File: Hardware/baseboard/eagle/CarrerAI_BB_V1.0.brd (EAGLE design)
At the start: 59 x 52 mm, 190 parts, among them J1 MICROUSB-FEM, X1 JST-4POS-2X4POS, X1.2 TACH/LAP, X2.2 VRAILS+, X2.3 5V+SoC

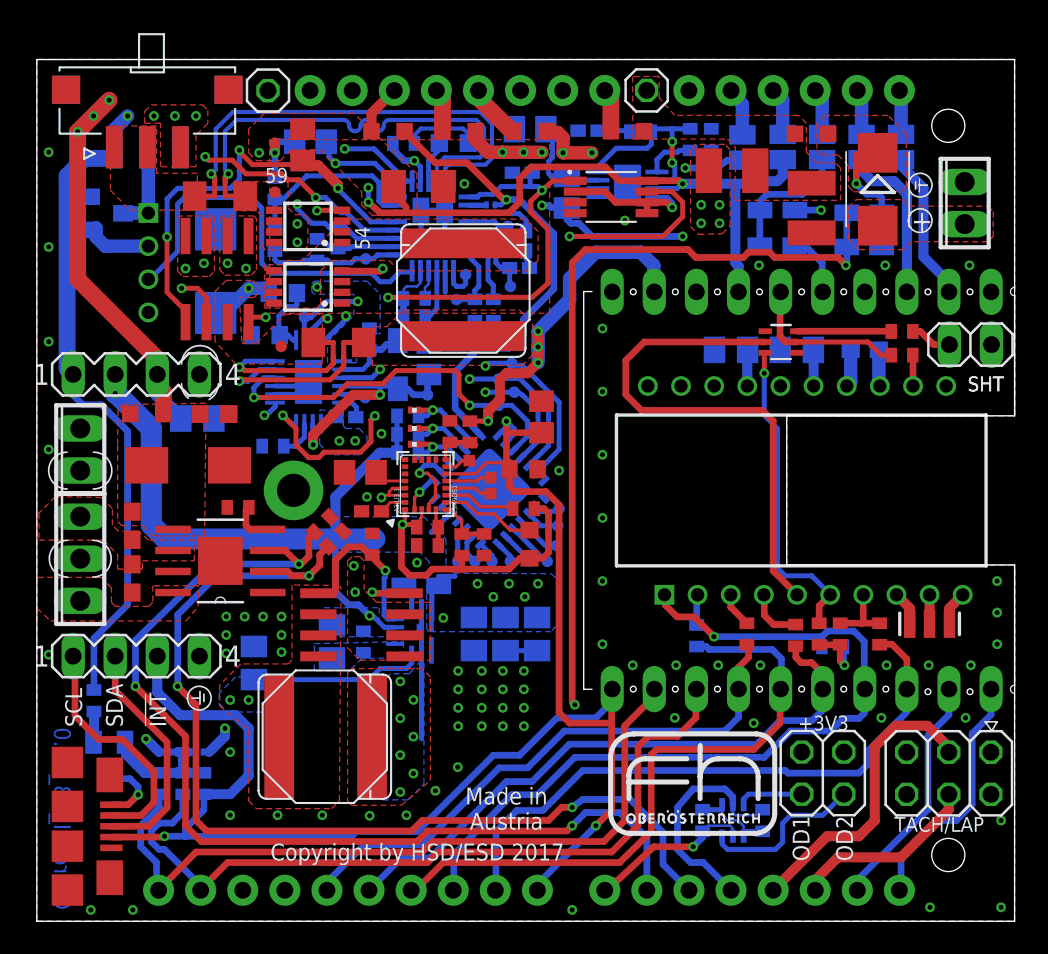
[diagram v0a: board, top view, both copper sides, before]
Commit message: CarrerAI_BB_V1.0: now diverging from original design  -> will drop the management IC in favor of 100mil pitch vias     as it will result in a better and more flexible design     (can be patched against SoC side I/O, or topped with IC)  -> I2C GPIO can be attached via a mezzaine board     (there's enough space)  -> will repurpose some vias as pins in this area,     which was the intention from the start actually thinking of it
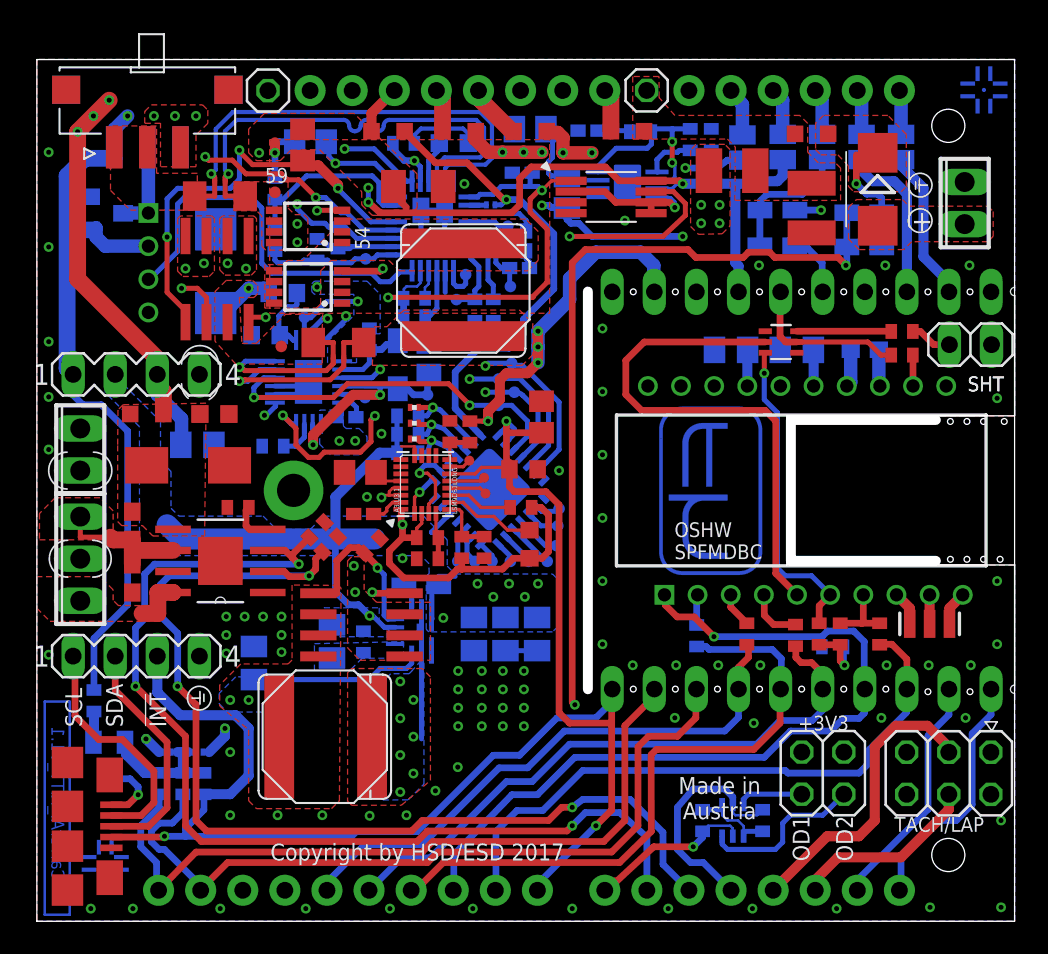
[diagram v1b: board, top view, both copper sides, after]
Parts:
- added U$1, U$2: (no value), marks:PASSER-CIRCLE
- A10:REF2: value REF.LOGO.UASUA -> REF.LOGO.UASUAS-GRADE; device kitt.refs:REF_LOGO_UASUA -> kitt.refs:DCL.LOGO.FHOOE-6MM-S
- A3:U3.1: value LSM9DS1 -> LSM9DS1LONG; device kitt.ic:LGA-24 -> kitt.ic:KITT.IC_LGA-24
- A3:☇1, A3:☇2, A3:☇3: value PTR1TP07SQ -> PTR1TP06R; device testpad:TP07SQ -> testpad:TP06R
- moved A10:REF2 22.5 mm to (40.6, 26.0), flipped to the bottom, turned to 270 degrees
- moved A7:DCL2 6.52 mm to (36.6, 22.9), flipped to the top
- moved A2:C1 1.59 mm to (9.68, 28.8)
- moved A3:R3.3 0.79 mm to (23.6, 21.9)
- moved A3:R3.6 0.63 mm to (23.6, 23.1)
- moved A3:C3.2 0.50 mm to (19.7, 24.6)
- moved A2:R1 0.45 mm to (16.9, 23.6)
- moved A2:R2 0.45 mm to (17.7, 22.8)
- moved A3:☇2 0.40 mm to (27.0, 26.8)
- moved A3:☇1 0.32 mm to (27.1, 25.8)
- moved A8:R2 0.32 mm to (22.8, 30.1)
- moved A8:R6 0.32 mm to (22.8, 29.1)
- moved A3:R3.2 0.18 mm to (29.2, 25.0)
- moved A3:R3.4 0.16 mm to (27.0, 22.6)
- moved A3:R3.5 0.16 mm to (25.6, 22.6)
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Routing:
- net N$14: track 0.00 -> 28.7 mm
- net +5V: track 91.6 -> 81.8 mm, vias 11 -> 10
- net ✳TOP.MOT+: track 0.00 -> 8.38 mm
- net TOP.MOT-: track 0.00 -> 3.14 mm
- net PWR.MOTA: track 60.8 -> 62.9 mm
- net +18V: track 37.6 -> 39.2 mm
- net GND: track 27.8 -> 29.2 mm, vias 74 -> 82
- net TOP.RUN: track 23.6 -> 22.3 mm
- net PWR.MOTB: track 61.5 -> 62.8 mm
- net A3:DRDY_M: track 3.21 -> 2.29 mm
- net +3V3: track 73.4 -> 74.3 mm
- net A10:BATOK: track 8.73 -> 9.57 mm
- net A3:INT_M: track 2.80 -> 2.16 mm
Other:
- outline, holes or cut-outs redrawn
- board text added: "CarrerAI_KITT_V1.1"
- board text removed: "CarrerAI_BB_V1.0"

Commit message: BB-SRII: pretty much, out of the blue, the gyro area opti/minimized itself
looks nice
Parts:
- removed A8:IC1: MCP23017ML, microchip:QFN28-ML_6X6MM
- removed A8:R1, A8:R3, A8:R5: 10kR/⎒, rcl:R0402
- removed A8:R2: 10kR/⎑, rcl:R0201
- removed A8:R4, A8:R6: 10kR/⎒, rcl:R0201
- removed A8:TP2, A8:TP3, A8:TP4, TP2, TP3, TP4, TP5, TP6, TP7: TPTP07R, testpad:TP07R
- added A3:C3.3, A3:C3.4, A3:C3.5: 100nF/⇤, rcl:C0402K
- added X5: 87758-0816, con-molex:87758-0816
- added X6: 87758-0616, con-molex:87758-0616
- A3:R3.1: device rcl:R0603 -> resistor:R0402
- A3:R3.11, A3:R3.3, A3:R3.4: device rcl:R0402 -> rcl:R0201
- A3:R3.2: device rcl:R0402 -> resistor:R0402
- moved A3:R3.6 9.45 mm to (31.0, 29.1), flipped to the bottom
- moved A3:R3.3 9.07 mm to (29.1, 29.1), flipped to the bottom, turned to 90 degrees
- moved A3:R3.5 7.45 mm to (31.0, 27.8), flipped to the bottom, turned to 0 degrees
- moved A3:R3.10 7.42 mm to (31.0, 23.9), flipped to the bottom, turned to 0 degrees
- moved A3:R3.11 7.05 mm to (29.1, 23.9), flipped to the bottom, turned to 270 degrees
- moved A3:R3.4 5.64 mm to (29.1, 27.8), flipped to the bottom
- moved A3:C3.XX 4.33 mm to (26.7, 28.2), turned to 180 degrees
- moved A6:☇8 4.23 mm to (25.5, 34.6)
- moved A3:R3.1 3.88 mm to (31.0, 26.4), flipped to the bottom, turned to 0 degrees
- moved A9:C4 3.65 mm to (30.7, 20.9)
- moved A9:C3 3.63 mm to (28.6, 20.9)
- moved A9:C2 3.62 mm to (26.5, 20.9)
- moved A3:☇3 3.39 mm to (27.2, 24.6), flipped to the bottom
- moved A3:R3.9 2.90 mm to (26.7, 26.0), turned to 180 degrees
- moved A3:U3.1 2.71 mm to (25.5, 27.5), flipped to the bottom, turned to 270 degrees
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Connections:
- removed net A8:A0: A8:IC1.11, A8:R5.2, A8:R6.1
- removed net A8:A1: A8:IC1.12, A8:R1.2, A8:R2.1
- removed net A8:A2: A8:IC1.13, A8:R3.2, A8:R4.1
- removed net A8:N$3: A8:IC1.23, A8:TP2.TP
- removed net A8:N$4: A8:IC1.24, A8:TP3.TP
- removed net A8:N$5: A8:IC1.25, A8:TP4.TP
- removed net TOP1: A8:IC1.26, TP2.TP
- removed net TOP2: A8:IC1.27, TP3.TP
- removed net TOP3: A8:IC1.28, TP4.TP
- removed net TOP4: A8:IC1.1, TP5.TP
- removed net TOP5: A8:IC1.2, TP6.TP
- removed net TOP6: A8:IC1.3, TP7.TP
- removed net TOP7: A8:IC1.4
- net +3V3: now also A3:C3.3.1, A3:C3.4.1, A3:C3.5.1, X6.5, X6.6
- net +5V: no longer A8:IC1.5, A8:R1.1, A8:R3.1, A8:R5.1
- net GND: now also A3:C3.3.2, A3:C3.4.2, A3:C3.5.2; no longer A8:IC1.6, A8:R2.2, A8:R4.2, A8:R6.2
- net SYSTWI.!INT: no longer A8:IC1.15, A8:IC1.16
- net SYSTWI.SCL: no longer A8:IC1.8
- net SYSTWI.SDA: no longer A8:IC1.9
- net TOP.!RST: no longer A8:IC1.14
- net TOP.FREQ: no longer A8:IC1.19
- net TOP.MODE: no longer A8:IC1.18
- net TOP.PGOOD: no longer A8:IC1.20
- net TOP.RUN: no longer A8:IC1.17
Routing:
- net +5V: track 81.8 -> 48.7 mm, vias 10 -> 5
- net +3V3: track 74.3 -> 41.5 mm, vias 11 -> 9
- net TOP.MODE: track 27.1 -> 1.13 mm, vias 2 -> 1
- net TOP.PGOOD: track 24.4 -> 1.83 mm, vias 2 -> 1
- net TOP.FREQ: track 26.6 -> 10.0 mm, vias 3 -> 2
- net GND: track 29.2 -> 41.8 mm, vias 82 -> 75
- net SYSTWI.!INT: track 100.9 -> 90.1 mm
- net TOP.RUN: track 22.3 -> 12.3 mm, vias 2 -> 1
- net TOP.!RST: track 67.7 -> 61.2 mm
- net A8:A2: track 5.25 -> 0.00 mm, vias 1 -> 0
- net SYSTWI.SCL: track 110.4 -> 105.1 mm, vias 1 -> 0
- net A8:A1: track 4.60 -> 0.00 mm, vias 1 -> 0
- net A8:A0: track 4.16 -> 0.00 mm, vias 1 -> 0
- net SYSTWI.SDA: track 108.2 -> 104.5 mm, vias 1 -> 0
- net A3:SDO_AG: track 2.76 -> 6.31 mm
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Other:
- outline, holes or cut-outs redrawn
- board text added: "OVERFIT DISCARD GET OUTTA HERE"
- board text added: "eureka!"
- board text added: "hold it! make breakaway , really ridicuously long jumper PCB!"
- board text added: "label bias lines!"
- board text added: "make PD Jmpers 0201"
- board text added: "mount on bottom"
- board text added: "need to split planes again for sensor core eh meh"
- board text added: "place tname -> "gumstick" and "core" interfaces"
- board text added: "who ruled that these should be 0402? ech."

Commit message: BB-SRII: minor fixes, in process of dropping the fat good for nothin' pmos
the weather is nice outside
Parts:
- removed A10:T1: SI4427BDY, kitt.ic:SOIC8
- moved J1 66.9 mm to (67.2, 9.38)
- moved A6:☇6 18.3 mm to (28.7, 16.0)
- moved A6:☇9 14.8 mm to (13.7, 29.5), flipped to the top
- moved A6:☇8 10.3 mm to (15.6, 31.6), flipped to the top
- moved A6:☇7 8.45 mm to (20.9, 36.6)
- moved A7:DCL2 5.56 mm to (36.4, 17.3)
- moved A9:R3 4.13 mm to (24.3, 22.1), turned to 270 degrees
- moved A5:☇7 0.81 mm to (28.7, 37.5)
- moved A5:C5 0.67 mm to (30.0, 40.6)
- moved A5:C6 0.65 mm to (29.3, 38.8)
- moved A9:R2 0.58 mm to (18.7, 16.3)
- moved A5:☇3 0.57 mm to (28.7, 41.5)
- moved A5:☇2 0.45 mm to (28.7, 40.4)
- moved A3:R3.3 0.32 mm to (29.1, 29.4)
- moved A3:R3.6 0.32 mm to (31.0, 29.4)
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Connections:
- new net TOP.5VEN: A9:R3.2, A9:U1.7, X5.3
- net +5V: now also X5.2
- net A10.!ACT: now also X5.7; no longer A10:T1.4
- net GND: now also X5.4, X5.6, X5.8
- net TOP.!RST: now also X6.4
- net TOP.PGOOD: now also X6.1
- net TOP.RUN: now also X6.2
- net TOP.VSYS/GUARD: now also X5.1; no longer A10:T1.5, A10:T1.6, A10:T1.7, A10:T1.8, A9:C1.1, A9:L1.1, A9:R3.2, A9:U1.3, A9:U1.7
- net VDD: now also A9:C1.1, A9:L1.1, A9:U1.3; no longer A10:T1.1, A10:T1.2, A10:T1.3
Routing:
- net +4.1V: track 105.7 -> 84.3 mm
- net TOP.VSYS/GUARD: track 20.4 -> 0.00 mm, vias 3 -> 2
- net +5V: track 48.7 -> 65.5 mm, vias 5 -> 4
- net GND: track 41.8 -> 25.5 mm
- net TOP.PGOOD: track 1.83 -> 13.7 mm, vias 1 -> 2
- net SYSTWI.SCL: track 105.1 -> 93.4 mm, vias 0 -> 1
- net +3V3: track 41.5 -> 53.0 mm
- net SYSTWI.SDA: track 104.5 -> 94.0 mm, vias 0 -> 1
- net TOP.5VEN: track 0.00 -> 10.2 mm, vias 0 -> 1
- net TOP.FREQ: track 10.0 -> 16.6 mm, vias 2 -> 1
- net N$1: track 4.29 -> 0.00 mm, vias 1 -> 0
- net TOP.RUN: track 12.3 -> 16.4 mm
- net A6:TRACK/SS: track 2.27 -> 0.00 mm
- net N$4: track 1.87 -> 0.04 mm
- net A10.!ACT: track 38.2 -> 36.4 mm, vias 2 -> 0
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- removed copper zone on layer 15, net +5V
- removed copper zone on layer 1, net TOP.VSYS/GUARD
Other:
- board text added: "#1-DOMH #2-AAAA #3-... #4-... #5-... #6-..."
- board text added: "1720"
- board text added: "OSHW/SPFMDBC"
- board text added: "TPIC2810 here"
- board text added: "YA WANT LEDS? PLACE .... oh fuck off TI"
- board text added: "delete nfet drivers, replace with straight up GPIO -> IO west and east finally"
- board text added: "don't forget SVEN bias config!"
- board text added: "don't forget to set diameter for pinheads after library finish"
- board text added: "everyone sign with initials here?"
- board text added: "finally redo this hot garbage"
- board text added: "finishing touch QR HERE TO REPO path @ REVISION literally 5min using ULP script"
- board text added: "idk what to put here."
- board text added: "tie twi bus voltage to gnd here move gnd symbol to right"
- board text added: "trash piece gets layer guide"
- board text added: "why?"
- board text removed: "make PD Jmpers 0201"
- board text removed: "who ruled that these should be 0402? ech."

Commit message: CarrerAI BB SV2: it dowsn't look like much has changed but there has been some progress.
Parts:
- removed A10:U2: 2NANDSOP8, kitt.ic:SOP65P490X110-8N
- removed A7:J1: (no value), pinhead:1X02
- removed J1: MICROUSB-FEM, kitt.con:10118192-0001LF
- added A7:J2: 22-27-2021-02, con-molex:6410-02
- added A7:X1: 87758-0216, con-molex:87758-0216
- added A9:R4: ~10kR/⎵, resistor:R0402
- added A9:R5: (no value), rcl:R0201
- added LED1: VINS, led:CHIP-LED0805
- added LED2: VSYS, led:CHIP-LED0805
- added LED3: 5VCC, led:CHIP-LED0805
- added LED4: 3VCC, led:CHIP-LED0805
- added LED5: PROBLEM, led:CHIP-LED0805
- added PAD1, PAD2: (no value), wirepad:1,6/0,9
- added R8: 100R, rcl:R0402
- added SV3: (no value), con-lsta:FE05-2W
- added X3: 87758-1016, con-molex:87758-1016
- A9:R3: value 100kR/⎵ -> 1MR/⎵
- X2.3: value 5V+SoC -> SoC
- moved A10:R3 31.9 mm to (19.5, 17.6), flipped to the top, turned to 90 degrees
- moved A10:R2 30.4 mm to (24.8, 20.6), flipped to the top, turned to 180 degrees
- moved A10:R4 30.3 mm to (17.1, 17.6), flipped to the top
- moved A10:R7 29.6 mm to (27.8, 20.6), flipped to the top, turned to 180 degrees
- moved A10:R1 27.8 mm to (24.8, 22.5), flipped to the top
- moved A10:U1 27.4 mm to (20.3, 21.7), flipped to the top, turned to 0 degrees
- moved A10:C1 25.8 mm to (27.8, 22.5), flipped to the top
- moved A6:☇6 14.8 mm to (18.8, 27.1), flipped to the top
- moved A6:☇7 6.12 mm to (14.8, 36.2), flipped to the top
- moved A9:R3 3.96 mm to (23.0, 18.4), turned to 90 degrees
- moved A2:R2 3.54 mm to (16.0, 25.9), turned to 270 degrees
- moved A2:R1 3.11 mm to (14.6, 25.7), turned to 90 degrees
- moved A5:C4 3.03 mm to (26.7, 43.7), flipped to the top, turned to 180 degrees
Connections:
- net N$7 renamed UNO.ADC3
- net N$8 renamed UNO.ADC2
- net N$9 renamed UNO.ADC1
- removed net A10:BATOK: A10:U1.8, A10:U2.2, A10:U2.5, A10:U2.6
- removed net A10:REF: A10:R1.2, A10:R2.1, A10:U1.4, A10:U1.6
- removed net TOP.!BATOK: A10:U2.3
- removed net TOP.PWRON: A10:U2.1, A5:C4.1, A5:R11.2, A5:R12.2, A5:U1.1, A5:U1.13
- removed net TOP.VSYS/GUARD: X5.1
- new net A10:IN+&REF: A10:R1.2, A10:R2.1, A10:U1.3, A10:U1.6
- new net A5:BIAS: A5:C4.1, A5:R11.2, A5:R12.2, A5:U1.1, A5:U1.13
- net +18V: now also A4:C1.1, A4:F1.1, A4:L1.2, A4:R3.2, JP1.1, L4.1, PAD1.1, PAD2.1
- net +24V: no longer A4:C1.1, A4:F1.1, A4:L1.2, A4:R3.2, JP1.1, L4.1
- net +3V3: now also A7:X1.2; no longer A7:J1.1
- net +4.1V: no longer A10:R4.2
- net A10.!ACT: no longer A10:U2.7
- net A10:IN-: now also A10:U1.4; no longer A10:U1.3
- net A7:N$8: now also A7:X1.1; no longer A7:J1.2
- net GND: no longer A10:U2.4, J1.5, J1.M1, J1.M2, J1.S1, J1.S2, J1.S3, J1.S4
- net N$1: no longer J1.1
- net SYSTWI.!INT: no longer J1.4
- net SYSTWI.SCL: no longer J1.2
- net SYSTWI.SDA: no longer J1.3
- net TOP.5VEN: now also A10:U1.8, A9:R4.1, A9:R5.1, A9:R5.2
- net TOP.FREQ: now also X5.5
- net TOP.MODE: now also X6.3
- net VDD: now also A10:R4.2, A9:R4.2, X5.1; no longer A10:U2.8
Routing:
- net A10.!ACT: track 36.4 -> 0.00 mm
- net A10:IN+&REF: track 0.00 -> 30.8 mm
- net TOP.PWRON: track 28.9 -> 0.00 mm, vias 2 -> 0
- net +4.1V: track 84.3 -> 61.8 mm, vias 7 -> 5
- net VDD: track 47.1 -> 64.8 mm, vias 17 -> 19
- net TOP.5VEN: track 10.2 -> 26.5 mm, vias 1 -> 2
- net A10:REF: track 11.9 -> 0.00 mm, vias 2 -> 0
- net TOP.MODE: track 2.13 -> 14.0 mm
- net A10:BATOK: track 9.57 -> 0.00 mm, vias 1 -> 0
- net TOP.FREQ: track 16.6 -> 7.80 mm, vias 1 -> 0
- net A5:BIAS: track 0.00 -> 8.57 mm, vias 0 -> 1
- net +3V3: track 53.0 -> 60.7 mm, vias 9 -> 8
- net +18V: track 39.2 -> 46.8 mm
- net +5V: track 65.5 -> 59.1 mm, vias 4 -> 3
- net DDC.CLN/VIN: track 1.14 -> 4.91 mm
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- added copper zone on layer 1, net +18V
- added copper zone on layer 15, net +18V
- added copper zone on layer 16, net +18V
- added copper zone on layer 2, net +18V
- added copper zone on layer 16, net VDD
- removed copper zone on layer 1, net +24V
- removed copper zone on layer 16, net DDC.CLN/VIN
- removed copper zone on layer 16, net TOP.VSYS/GUARD
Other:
- board size 59 x 52 mm -> 59 x 55 mm
- board text added: "3V"
- board text added: "3VCC"
- board text added: "5VCC"
- board text added: "A"
- board text added: "B"
- board text added: "FABHOUSE AREA"
- board text added: "GRADOS Generic Robotic Automation Developer Open-Hardware System"
- board text added: "KITT evolves into"
- board text added: "LAYER GUIDE"
- board text added: "OD"
- board text added: "PROBLEM"
- board text added: "SHUT"
- board text added: "SYSTEWI"
- board text added: "VINS"
- board text added: "VSYS"
- board text added: "WANT LEDS? PLACE .... oh kack off TI"
- board text added: "XTRA FUL SYSTEWI"
- board text added: "do it yourself if you need extra user leds ffs man dont stick it to the man"
- board text added: "for tracer"
- board text removed: "!INT"
- board text removed: "#1-DOMH #2-AAAA #3-... #4-... #5-... #6-..."
- board text removed: "+3V3"
- board text removed: "51"
- board text removed: "52"
- board text removed: "53"
- board text removed: "54"
- board text removed: "56"
- board text removed: "62"
- board text removed: "65"
- board text removed: "66"
- board text removed: "67"
- board text removed: "68"
- board text removed: "69"
- board text removed: "OD1"
- board text removed: "OD2"
- board text removed: "SCL"
- board text removed: "SDA"
- board text removed: "SHT"
- board text removed: "TACH/LAP"
- board text removed: "VIN"
- board text removed: "YA WANT LEDS? PLACE .... oh fuck off TI"
